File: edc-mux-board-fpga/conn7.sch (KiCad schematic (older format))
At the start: 24 parts, among them U25 MAX4910, U26 TLV320AIC3206, U27 P82B96

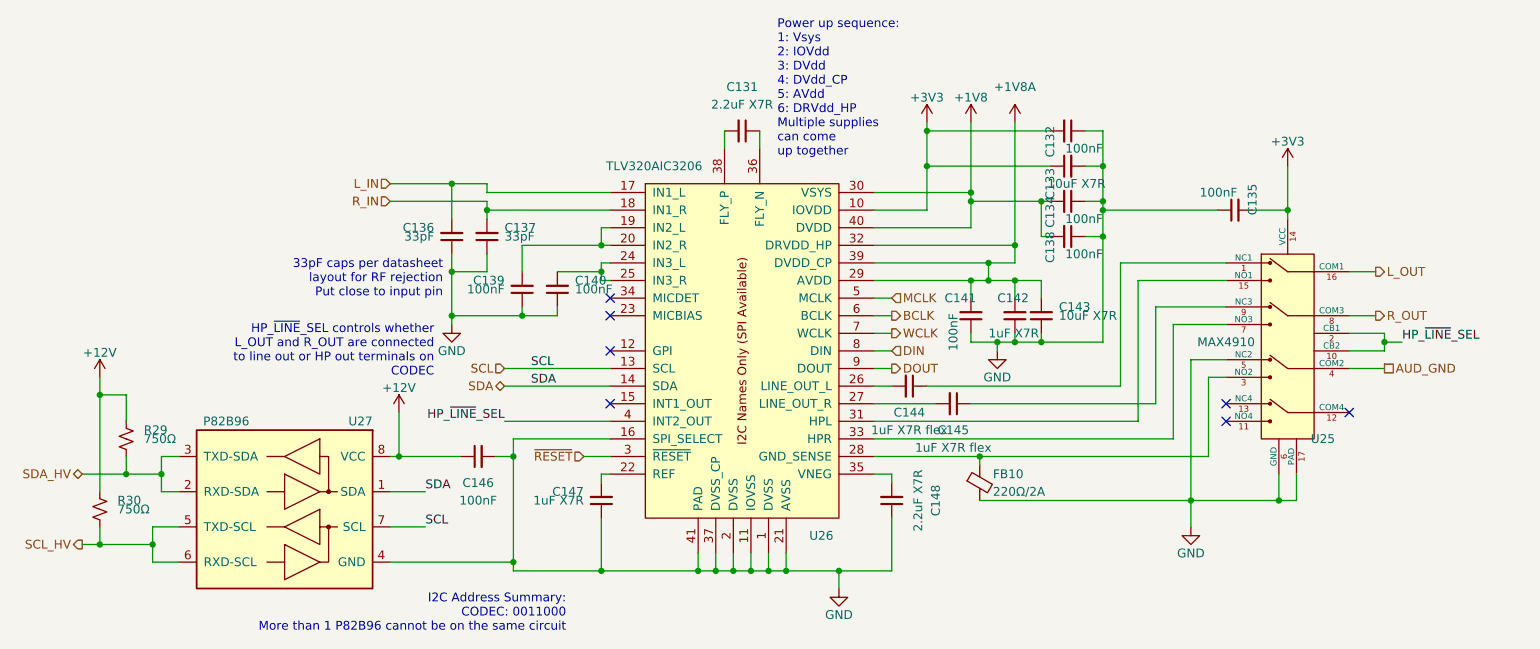
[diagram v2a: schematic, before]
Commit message: re-annotating after adding power ICs and decoupling capacitors.
Also verified most footprints, and updated schematic field data.
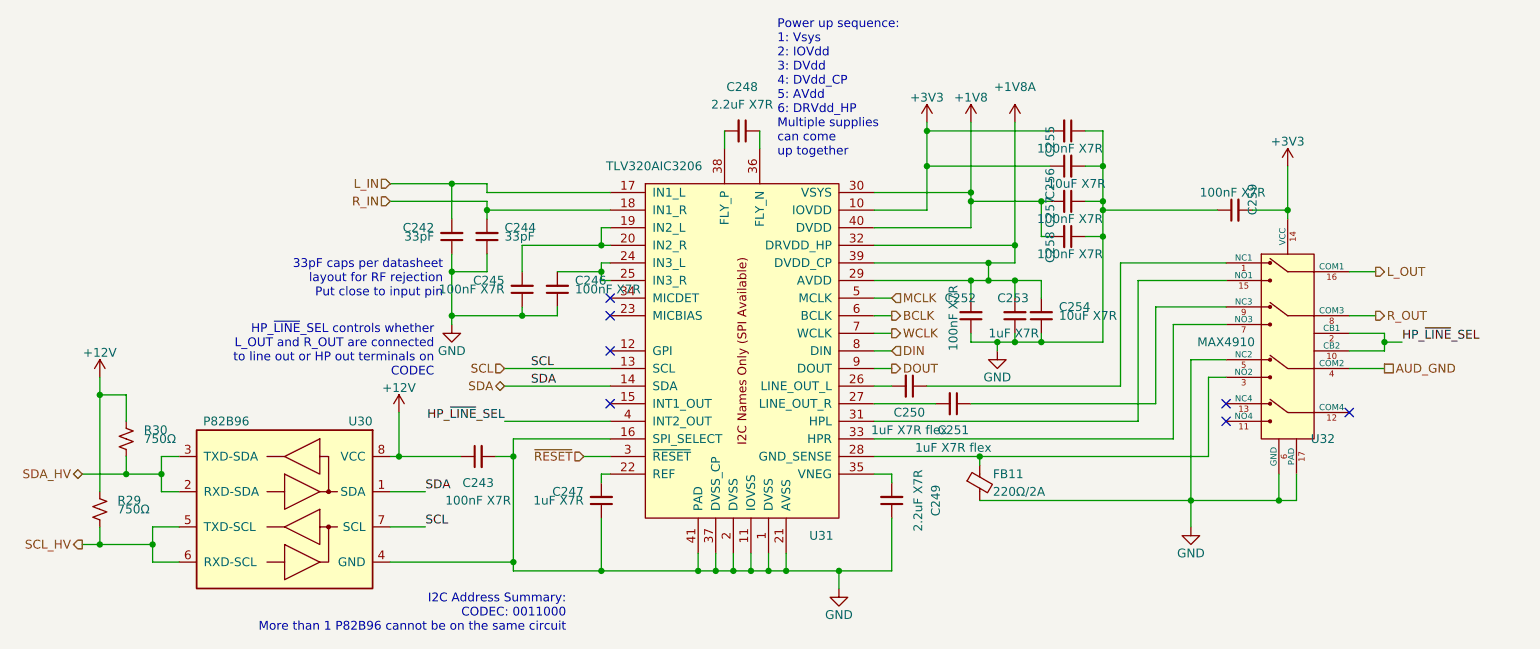
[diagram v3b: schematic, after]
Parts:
- C243: renamed from C146; value 100nF -> 100nF X7R
- C245: renamed from C139; value 100nF -> 100nF X7R
- C246: renamed from C140; value 100nF -> 100nF X7R
- C252: renamed from C141; value 100nF -> 100nF X7R
- C255: renamed from C132; value 100nF -> 100nF X7R
- C257: renamed from C134; value 100nF -> 100nF X7R
- C258: renamed from C138; value 100nF -> 100nF X7R
- C259: renamed from C135; value 100nF -> 100nF X7R
- R29: renamed from R30; Package ID (none) -> 0402in/1005mm
- R30: renamed from R29; Package ID (none) -> 0402in/1005mm
- renumbered C136 to C242, C137 to C244, C147 to C247, C131 to C248, C148 to C249, C144 to C250, C145 to C251, C142 to C253, C143 to C254, C133 to C256, FB10 to FB11, U27 to U30, U26 to U31, U25 to U32

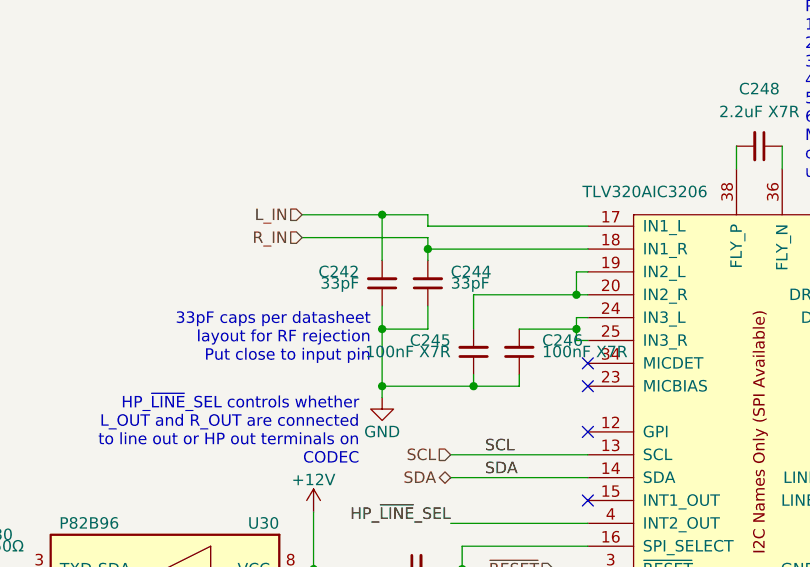
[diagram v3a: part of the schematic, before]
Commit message: Reannotating and adding more fields to components
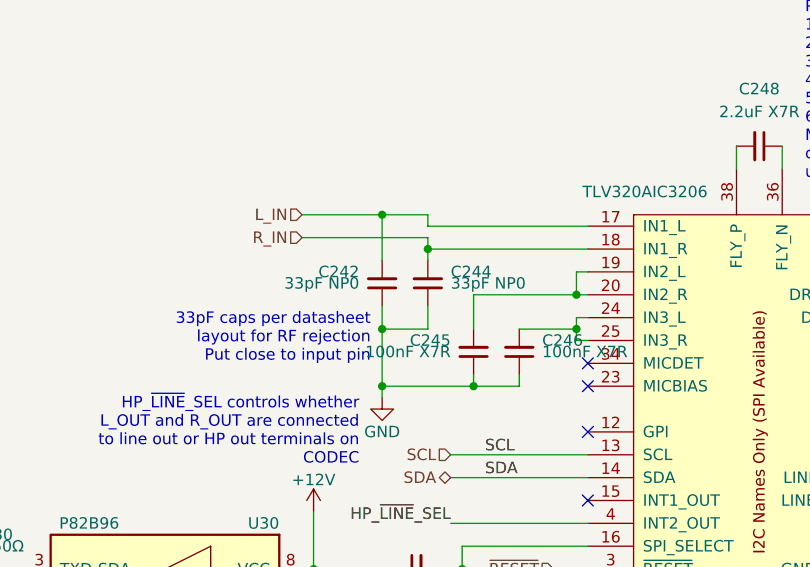
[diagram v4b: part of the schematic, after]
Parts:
- C242, C244: value 33pF -> 33pF NP0; footprint Capacitor_SMD:C_0603_1608Metric -> Capacitor_SMD:C_0402_1005Metric; Characteristics (none) -> CAP CER 33PF 25V NP0 0402; Description (none) -> MLCC Capacitor; Manufacturer (none) -> AVX; Manufacturers Part Number (none) -> 04023A330FAT2A; Package ID 0603in/1608mm -> 0402in/1005mm
- C243, C245, C246, C252, C255, C257, C258, C259: Characteristics (none) -> CAP CER 0.1UF 25V X7R 0603; Description (none) -> MLCC Capacitor; Manufacturer (none) -> Kemet; Manufacturers Part Number (none) -> C0603C104J3RACAUTO
- C247, C253: Characteristics (none) -> CAP CER 1UF 25V X7R 0603; Description (none) -> MLCC Capacitor
- C248, C249: footprint Capacitor_SMD:C_0603_1608Metric -> Capacitor_SMD:C_0805_2012Metric; Characteristics (none) -> CAP CER 2.2UF 25V X7R 0805; Description (none) -> MLCC Capacitor; Manufacturer (none) -> TDK; Manufacturers Part Number (none) -> CGA4J3X7R1E225K125AB; Package ID 0603in/1608mm -> 0805in/2012mm
- C250, C251: Characteristics (none) -> CAP CER 0805 1UF 25V X7R 5%; Description (none) -> MLCC Capacitor; Manufacturers Part Number C0805X105J3RACAUTO -> C0805X105J3RECAUTO
- C254, C256: Characteristics (none) -> CAP CER 10UF 25V X7R 1206; Description (none) -> MLCC Capacitor
- FB11: footprint Resistor_SMD:R_0603_1608Metric -> Inductor_SMD:L_0603_1608Metric; Description (none) -> Ferrite Bead
- R29, R30: Description (none) -> Resistor
- U30: Description (none) -> I2C Buffer / Voltage Translator; Manufacturer (none) -> Texas Instruments; Manufacturers Part Number (none) -> P82B96; Package ID (none) -> TSSOP8
- U31: Description (none) -> I2S Audio Codec; Manufacturer (none) -> Texas Instruments; Package ID (none) -> UQFN40
- U32: Description (none) -> Clickless Audio Switch; Manufacturer (none) -> Maxim Integrated; Package ID (none) -> TQFN16

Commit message: Fixed resistor footprint
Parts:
- R29, R30: footprint Resistor_SMD:R_0603_1608Metric -> Resistor_SMD:R_0402_1005Metric
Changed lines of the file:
@@
 F 0 "R30" H 1800 3950 50  0000 L CNN
 F 1 "750Ω" H 1800 3900 50  0000 L CNN
-F 2 "Resistor_SMD:R_0603_1608Metric" H 1700 3900 50  0001 C CNN
+F 2 "Resistor_SMD:R_0402_1005Metric" H 1700 3900 50  0001 C CNN
 F 3 "~" H 1700 3900 50  0001 C CNN
 F 4 "0402in/1005mm" H 0   0   50  0001 C CNN "Package ID"
@@
 F 0 "R29" H 1650 4350 50  0000 L CNN
 F 1 "750Ω" H 1650 4300 50  0000 L CNN
-F 2 "Resistor_SMD:R_0603_1608Metric" H 1550 4300 50  0001 C CNN
+F 2 "Resistor_SMD:R_0402_1005Metric" H 1550 4300 50  0001 C CNN
 F 3 "~" H 1550 4300 50  0001 C CNN
 F 4 "0402in/1005mm" H 0   0   50  0001 C CNN "Package ID"
